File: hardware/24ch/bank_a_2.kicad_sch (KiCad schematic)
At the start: 45 parts, among them U101 AD7124-8BCPZ, U102 ADT7310TRZ, U103 ADT7310TRZ

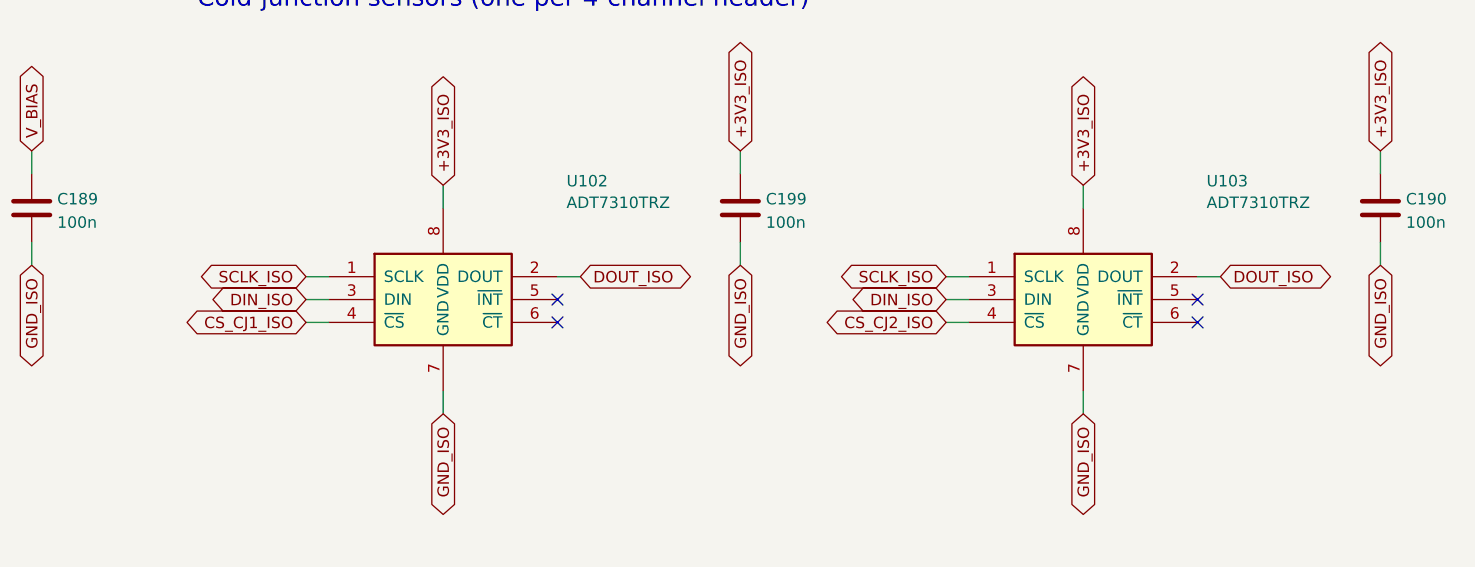
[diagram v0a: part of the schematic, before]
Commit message: 24ch cheaper-parts variant (0036): TMP126, CA-IS3761HW, RS-485 DNP, drop-in swaps
- CJ sensors ADT7310 x6 -> TMP126DCKR (C5219998); R443 22k DIN_ISO-DOUT_ISO for the
  3-wire SIO, R415 removed, ALERT grounded. Sensors moved <= 8 mm to clear spots beside
  their 100 nF (no closer spot to the terminals without touching TC traces, 0035 D2).
- ISO7761 -> CA-IS3761HW (same pinout, 5F/1R, default high); BOCHEN 3296W trimmer;
  SAMWHA 22u 1210.
- RS-485 block DNP: footprints kept; fab.py drops DNP parts from BOM/CPL and writes
  DNP.txt; cost.py skips them. External window watchdog tried and removed (owner).
- gen/delta.py: carry a schematic change onto the routed board (replace/add/remove,
  re-net, DNP, OLD>NEW@DEG reuse); it never deletes another net's track under a pad.
- Board: incremental edits only; analog nets (TC*, V_BIAS, VREF, REF*) identical to
  the pre-0036 board. Gates: ERC 0/0 (471 symbols); fab.py DRC/unconnected/parity
  0/0/0; pincaps 0 over. Parts ~$105 -> ~$72/board (CALCULATIONS 8.1, by hand).
- Docs: decision 0036, CALCULATIONS 8, ISSUES (I-109, I-114, I-119, I-104, I-094,
  new I-123 stock), STATE, 24ch README, superseded.txt.

Co-Authored-By: Claude Opus 5.5 <noreply@anthropic.com>
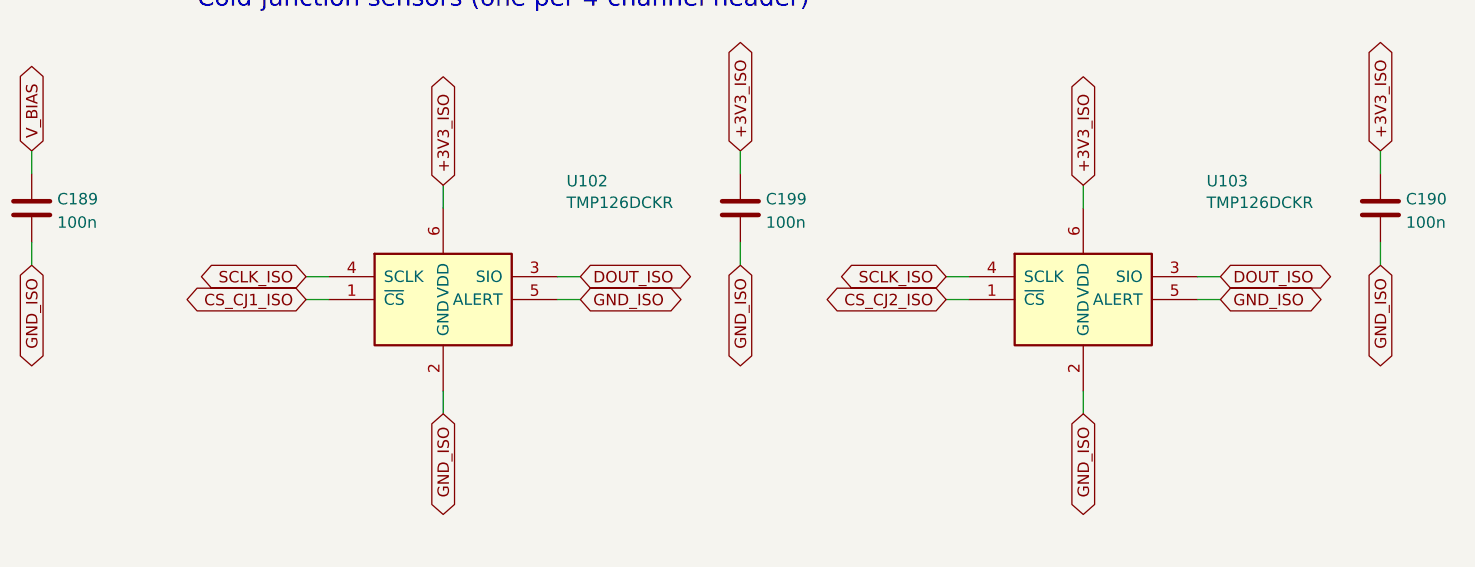
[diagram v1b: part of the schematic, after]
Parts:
- U102, U103: value ADT7310TRZ -> TMP126DCKR; footprint Package_SO:SOIC-8_3.9x4.9mm_P1.27mm -> Package_TO_SOT_SMD:SOT-363_SC-70-6; symbol thermo24:ADT7310 -> thermo24:TMP126; LCSC C578060 -> C5219998; MPN ADT7310TRZ-REEL7 -> TMP126DCKR; Manufacturer ADI -> TI
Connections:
- net +3V3_ISO: now also U102.6 (VDD), U103.6 (VDD); no longer U102.8 (VDD), U103.8 (VDD)
- net CS_CJ1_ISO: now also U102.1 (~{CS}); no longer U102.4 (~{CS})
- net CS_CJ2_ISO: now also U103.1 (~{CS}); no longer U103.4 (~{CS})
- net DIN_ISO: no longer U102.3 (DIN), U103.3 (DIN)
- net DOUT_ISO: now also U102.3 (SIO), U103.3 (SIO); no longer U102.2 (DOUT), U103.2 (DOUT)
- net GND_ISO: now also U102.2 (GND), U102.5 (ALERT), U103.2 (GND), U103.5 (ALERT); no longer U102.7 (GND), U103.7 (GND)
- net SCLK_ISO: now also U102.4 (SCLK), U103.4 (SCLK); no longer U102.1 (SCLK), U103.1 (SCLK)
- no-connect marks 6 -> 2
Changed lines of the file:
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@@
 	)
 	(symbol
-		(lib_id "thermo24:ADT7310")
+		(lib_id "thermo24:TMP126")
 		(at 251.46 182.88 0)
 		(unit 1)
@@
 			)
 		)
-		(property "Value" "ADT7310TRZ"
+		(property "Value" "TMP126DCKR"
 			(at 265.16 172.12 0)
 			(effects
@@
 			)
 		)
-		(property "Footprint" "Package_SO:SOIC-8_3.9x4.9mm_P1.27mm"
+		(property "Footprint" "Package_TO_SOT_SMD:SOT-363_SC-70-6"
 			(at 251.46 182.88 0)
 			(effects
@@
 			)
 		)
-		(property "Description" "cold junction at the seam of header J101"
+		(property "Description" "cold junction at header J101; SIO on DOUT, written through R443; ALERT unused, grounded (datasheet allows) (0036)"
 			(at 251.46 182.88 0)
 			(effects
@@
 			)
 		)
-		(property "MPN" "ADT7310TRZ-REEL7"
+		(property "MPN" "TMP126DCKR"
 			(at 251.46 182.88 0)
 			(effects
@@
 			)
 		)
-		(property "Manufacturer" "ADI"
+		(property "Manufacturer" "TI"
 			(at 251.46 182.88 0)
 			(effects
@@
 			)
 		)
-		(property "LCSC" "C578060"
+		(property "LCSC" "C5219998"
 			(at 251.46 182.88 0)
 			(effects
@@
 			)
 		)
+		(pin "4"
+		)
 		(pin "1"
 		)
 		(pin "3"
 		)
-		(pin "4"
+		(pin "5"
+		)
+		(pin "6"
 		)
 		(pin "2"
-		)
-		(pin "5"
-		)
-		(pin "6"
-		)
-		(pin "8"
-		)
-		(pin "7"
 		)
 		(instances
@@
 		)
 	)
-	(global_label "DIN_ISO"
+	(global_label "CS_CJ1_ISO"
 		(shape bidirectional)
 		(at 236.22 182.88 180)
@@
 		(property "Intersheetrefs" "${INTERSHEET_REFS}"
 			(at 236.22 182.88 0)
-			(effects
-				(font
-					(size 1.27 1.27)
-				)
-				(hide yes)
-			)
-		)
-	)
-	(wire
-		(pts
-			(xy 238.76 185.42)
-			(xy 236.22 185.42)
-		)
-		(stroke
-			(width 0)
-			(type default)
-		)
-	)
-	(global_label "CS_CJ1_ISO"
-		(shape bidirectional)
-		(at 236.22 185.42 180)
-		(fields_autoplaced yes)
-		(effects
-			(font
-				(size 1.27 1.27)
-			)
-			(justify right)
-		)
-		(property "Intersheetrefs" "${INTERSHEET_REFS}"
-			(at 236.22 185.42 0)
 			(effects
 				(font
@@
 		)
 	)
-	(no_connect
-		(at 264.16 182.88)
-	)
-	(no_connect
-		(at 264.16 185.42)
+	(wire
+		(pts
+			(xy 264.16 182.88)
+			(xy 266.7 182.88)
+		)
+		(stroke
+			(width 0)
+			(type default)
+		)
+	)
+	(global_label "GND_ISO"
+		(shape bidirectional)
+		(at 266.7 182.88 0)
+		(fields_autoplaced yes)
+		(effects
+			(font
+				(size 1.27 1.27)
+			)
+			(justify left)
+		)
+		(property "Intersheetrefs" "${INTERSHEET_REFS}"
+			(at 266.7 182.88 0)
+			(effects
+				(font
+					(size 1.27 1.27)
+				)
+				(hide yes)
+			)
+		)
 	)
 	(wire
@@
 	)
 	(symbol
-		(lib_id "thermo24:ADT7310")
+		(lib_id "thermo24:TMP126")
 		(at 322.58 182.88 0)
 		(unit 1)
@@
 			)
 		)
-		(property "Value" "ADT7310TRZ"
+		(property "Value" "TMP126DCKR"
 			(at 336.28 172.12 0)
 			(effects
@@
 			)
 		)
-		(property "Footprint" "Package_SO:SOIC-8_3.9x4.9mm_P1.27mm"
+		(property "Footprint" "Package_TO_SOT_SMD:SOT-363_SC-70-6"
 			(at 322.58 182.88 0)
 			(effects
@@
 			)
 		)
-		(property "Description" "cold junction at the seam of header J102"
+		(property "Description" "cold junction at header J102; SIO on DOUT, written through R443; ALERT unused, grounded (datasheet allows) (0036)"
 			(at 322.58 182.88 0)
 			(effects
@@
 			)
 		)
-		(property "MPN" "ADT7310TRZ-REEL7"
+		(property "MPN" "TMP126DCKR"
 			(at 322.58 182.88 0)
 			(effects
@@
 			)
 		)
-		(property "Manufacturer" "ADI"
+		(property "Manufacturer" "TI"
 			(at 322.58 182.88 0)
 			(effects
@@
 			)
 		)
-		(property "LCSC" "C578060"
+		(property "LCSC" "C5219998"
 			(at 322.58 182.88 0)
 			(effects
@@
 			)
 		)
+		(pin "4"
+		)
 		(pin "1"
 		)
 		(pin "3"
 		)
-		(pin "4"
+		(pin "5"
+		)
+		(pin "6"
 		)
 		(pin "2"
-		)
-		(pin "5"
-		)
-		(pin "6"
-		)
-		(pin "8"
-		)
-		(pin "7"
 		)
 		(instances
@@
 		)
 	)
-	(global_label "DIN_ISO"
+	(global_label "CS_CJ2_ISO"
 		(shape bidirectional)
 		(at 307.34 182.88 180)
@@
 		(property "Intersheetrefs" "${INTERSHEET_REFS}"
 			(at 307.34 182.88 0)
-			(effects
-				(font
-					(size 1.27 1.27)
-				)
-				(hide yes)
-			)
-		)
-	)
-	(wire
-		(pts
-			(xy 309.88 185.42)
-			(xy 307.34 185.42)
-		)
-		(stroke
-			(width 0)
-			(type default)
-		)
-	)
-	(global_label "CS_CJ2_ISO"
-		(shape bidirectional)
-		(at 307.34 185.42 180)
-		(fields_autoplaced yes)
-		(effects
-			(font
-				(size 1.27 1.27)
-			)
-			(justify right)
-		)
-		(property "Intersheetrefs" "${INTERSHEET_REFS}"
-			(at 307.34 185.42 0)
 			(effects
 				(font
@@
 		)
 	)
-	(no_connect
-		(at 335.28 182.88)
-	)
-	(no_connect
-		(at 335.28 185.42)
-	)
-	(wire
+	(wire
+		(pts
+			(xy 335.28 182.88)
+			(xy 337.82 182.88)
+		)
+		(stroke
+			(width 0)
+			(type default)
+		)
+	)
+	(global_label "GND_ISO"
+		(shape bidirectional)
+		(at 337.82 182.88 0)
+		(fields_autoplaced yes)
+		(effects
+			(font
+				(size 1.27 1.27)
+			)
+			(justify left)
+		)
+		(property "Intersheetrefs" "${INTERSHEET_REFS}"
+			(at 337.82 182.88 0)
+			(effects
+				(font
+					(size 1.27 1.27)
+				)
+				(hide yes)
+			)
+		)
+	)
+	(wire
